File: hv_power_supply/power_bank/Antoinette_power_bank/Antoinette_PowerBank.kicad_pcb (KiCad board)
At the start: 2 copper layers, 30.5 x 48.3 mm, 44 parts, among them J1 NanoFit_RA_TH_02, J2 USB-Micro-1981568-1, J3 NanoFit_RA_TH_02, J4 USB-A-S-X-X-SM2, J5 NanoFit_RA_TH_02, Q1 SSM3K333R, U2 MCP73871T-2CCI_ML, U3 TPS61090RSAR

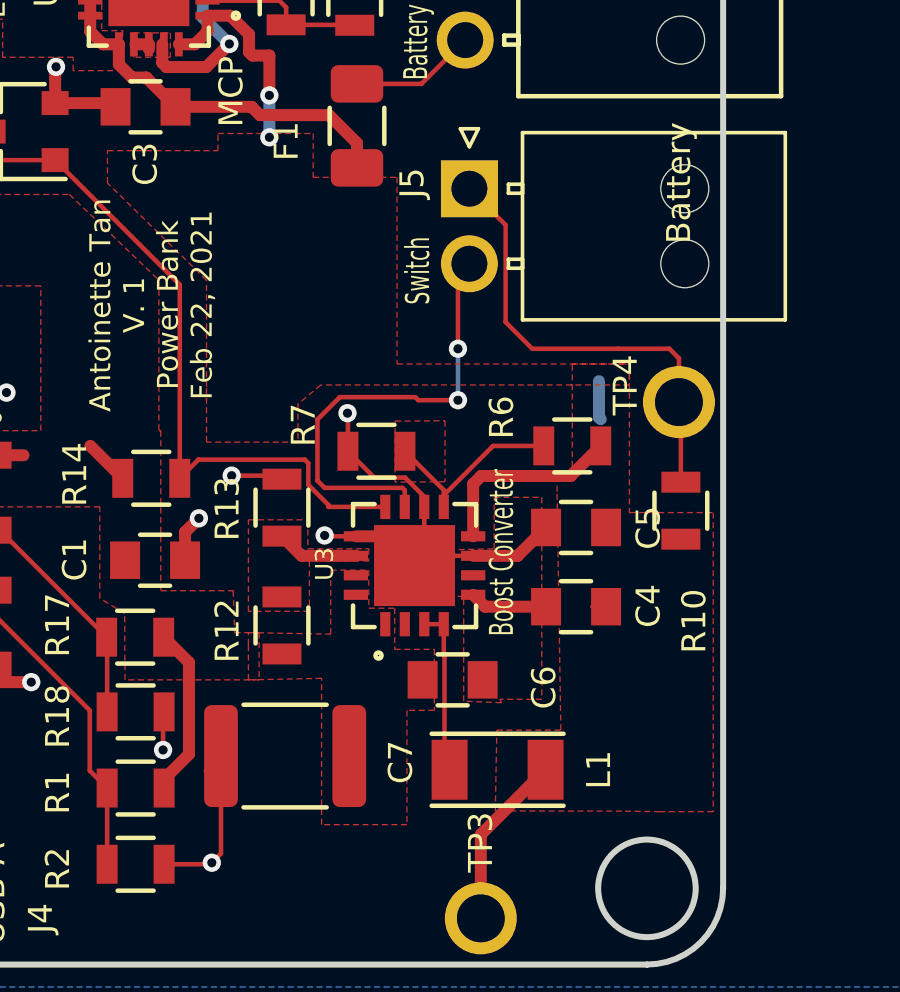
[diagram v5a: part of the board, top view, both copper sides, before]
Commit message: fixed library typos and adjusted silkscreen
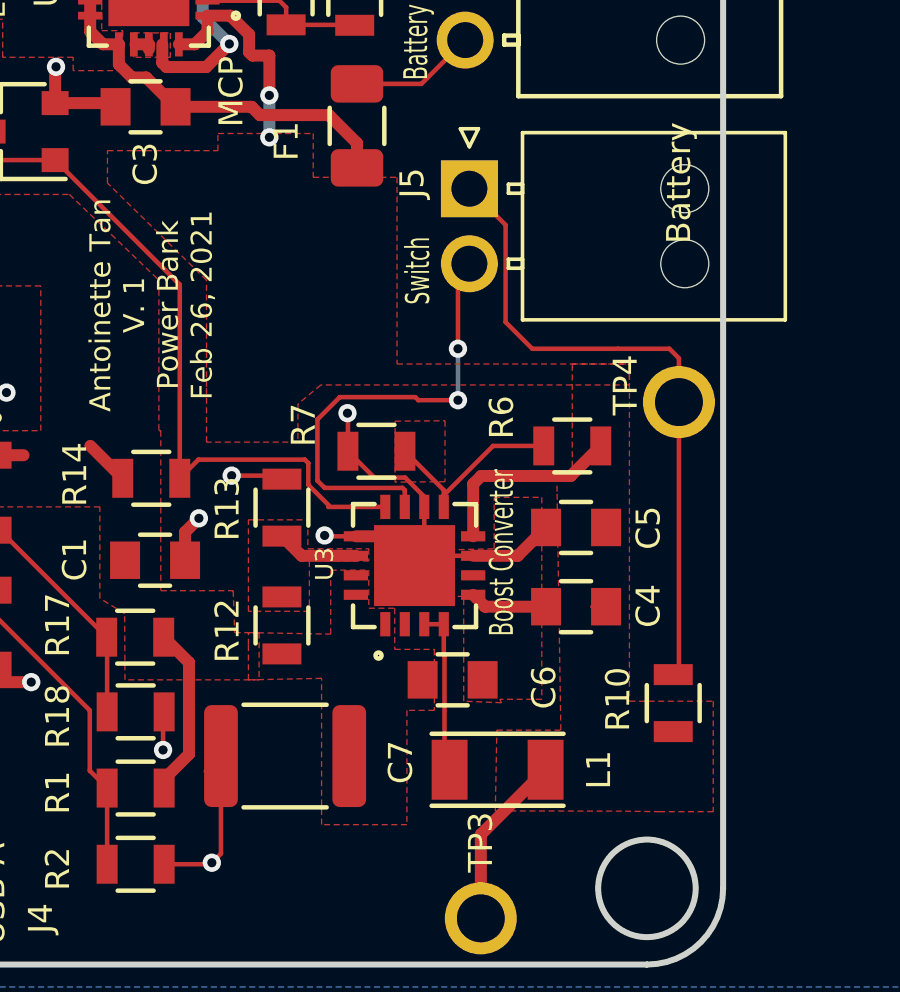
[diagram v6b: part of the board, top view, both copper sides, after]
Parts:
- moved R10 6.42 mm to (98.9, 69.3)
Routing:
- net Net-(J5-Pad1): track 15.6 -> 22.2 mm
- net +BATT: track 20.9 -> 19.6 mm
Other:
- board text added: "Antoinette Tan V. 1 Power Bank Feb 26, 2021"
- board text removed: "Antoinette Tan V. 1 Power Bank Feb 22, 2021"
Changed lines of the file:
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@@
     (thickness 1.6)
     (drawings 23)
-    (tracks 290)
+    (tracks 289)
     (zones 0)
     (modules 44)
@@
   )
   (module footprints:R_0805_OEM (layer F.Cu)
-    (at 99.187 62.865 90)
+    (at 98.933 69.2785 90)
     (descr "Resistor SMD 0805, reflow soldering, Vishay (see dcrcw.pdf)")
     (tags "resistor 0805")
     (attr smd)
-    (fp_text reference R10 (at -3.683 0.4445 90) (layer F.SilkS)
+    (fp_text reference R10 (at 0.127 -1.8415 90) (layer F.SilkS)
       (effects (font (size 0.8 0.8) (thickness 0.15)))
     )
@@
     (effects (font (size 0.8 0.5) (thickness 0.125)))
   )
-  (gr_text "Antoinette Tan\nV. 1\nPower Bank \nFeb 22, 2021\n" (at 81.534 56.007 90) (layer F.SilkS)
+  (gr_text "Antoinette Tan\nV. 1\nPower Bank \nFeb 26, 2021\n" (at 81.534 56.007 90) (layer F.SilkS)
     (effects (font (size 0.7 0.7) (thickness 0.175)))
   )
@@
   (segment (start 92.531499 61.708401) (end 92.2647 61.9752) (width 0.4) (layer F.Cu) (net 5))
   (segment (start 92.2647 63.7188) (end 92.2647 61.9752) (width 0.4) (layer F.Cu) (net 5))
-  (segment (start 96.4565 59.7535) (end 96.5175 59.8145) (width 0.4) (layer B.Cu) (net 5))
-  (segment (start 96.4565 58.547) (end 96.4565 59.7535) (width 0.4) (layer B.Cu) (net 5))
   (segment (start 84.167058 46.3644) (end 83.408799 46.3644) (width 0.4) (layer F.Cu) (net 5))
   (segment (start 84.794701 46.992043) (end 84.167058 46.3644) (width 0.4) (layer F.Cu) (net 5))
@@
   (segment (start 91.2847 66.6488) (end 91.2847 67.672318) (width 0.1524) (layer F.Cu) (net 27))
   (segment (start 99.187 59.309) (end 99.1235 59.2455) (width 0.1524) (layer F.Cu) (net 28))
-  (segment (start 99.187 61.915) (end 99.187 59.309) (width 0.1524) (layer F.Cu) (net 28))
   (segment (start 98.958399 59.080399) (end 99.1235 59.2455) (width 0.1524) (layer F.Cu) (net 28))
   (segment (start 99.1235 59.2455) (end 99.1235 57.785) (width 0.1524) (layer F.Cu) (net 28))
@@
   (segment (start 93.345 56.5785) (end 93.345 53.34) (width 0.15) (layer F.Cu) (net 28))
   (segment (start 97.0915 57.4675) (end 94.234 57.4675) (width 0.1524) (layer F.Cu) (net 28))
+  (segment (start 99.1235 68.138) (end 98.933 68.3285) (width 0.1524) (layer F.Cu) (net 28))
+  (segment (start 99.1235 59.2455) (end 99.1235 68.138) (width 0.1524) (layer F.Cu) (net 28))
   (segment (start 89.9847 62.7388) (end 89.9847 62.408798) (width 0.15) (layer F.Cu) (net 29))
   (segment (start 89.9847 62.1814) (end 89.908499 62.105199) (width 0.1524) (layer F.Cu) (net 29))
@@
       (pts
         (xy 93.0021 72.8726) (xy 93.0529 70.1802) (xy 95.1865 70.1802) (xy 95.0595 62.23) (xy 95.0595 61.722)
-        (xy 95.5675 61.722) (xy 95.5675 57.9755) (xy 97.4725 57.9755) (xy 97.4725 62.9285) (xy 100.2665 62.9285)
+        (xy 95.5675 61.722) (xy 95.5675 57.9755) (xy 97.4725 57.9755) (xy 97.4725 69.215) (xy 100.2665 69.215)
         (xy 100.2665 72.898) (xy 98.4885 72.898) (xy 97.2185 72.87963)
       )

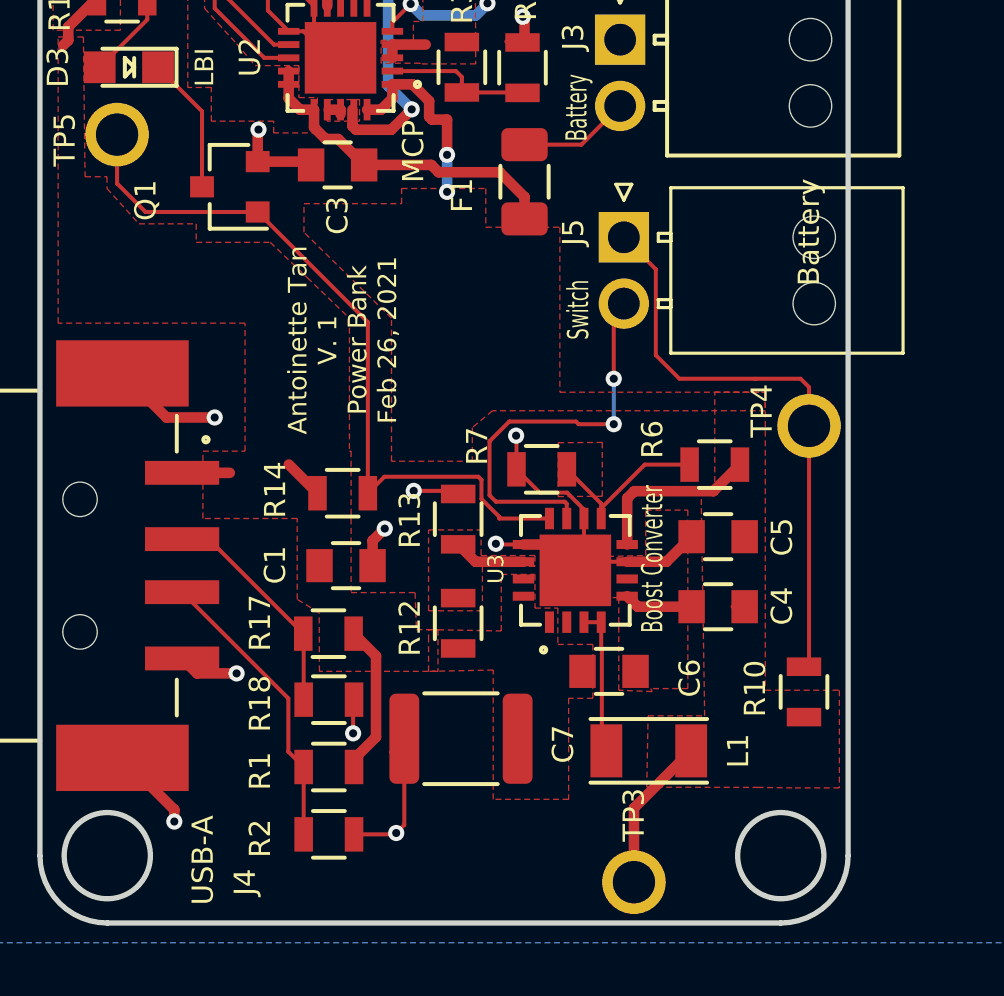
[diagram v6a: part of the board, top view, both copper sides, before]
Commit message: make silkscreen more legible
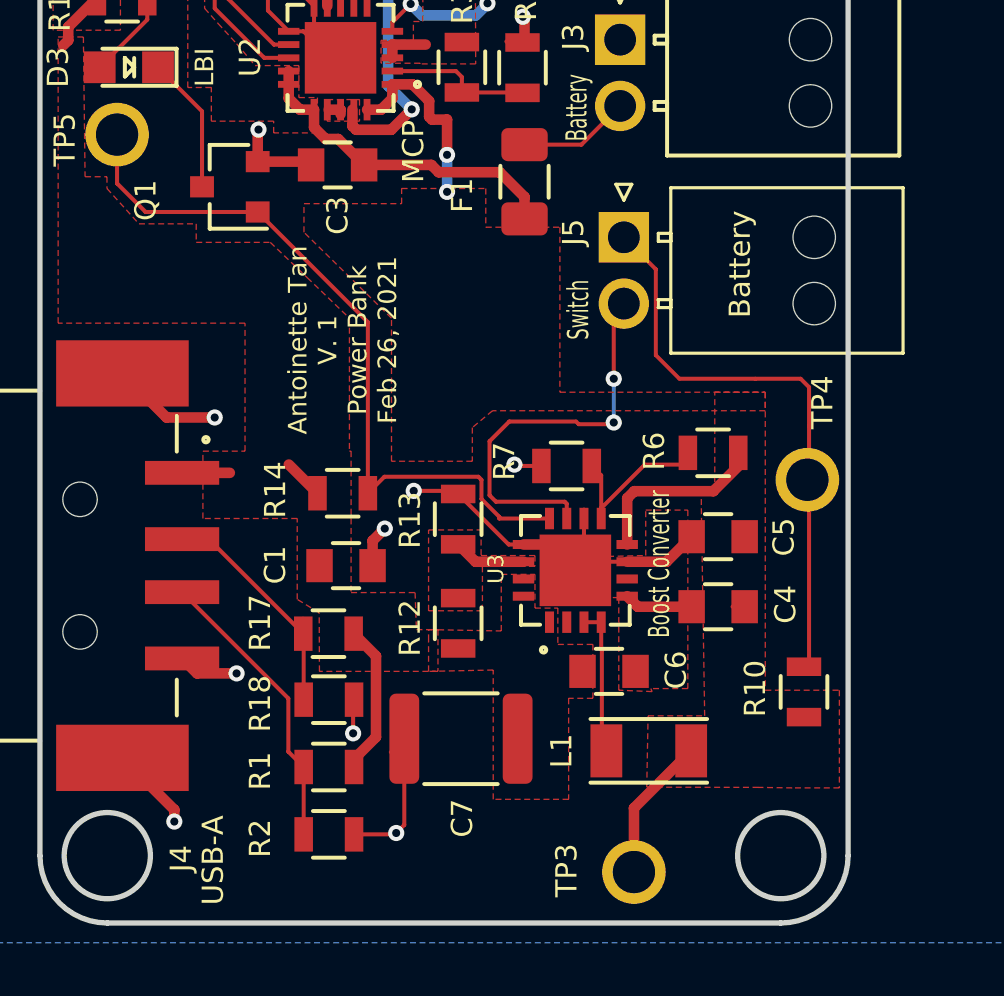
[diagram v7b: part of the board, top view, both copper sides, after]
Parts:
- moved TP4 2.03 mm to (99.1, 61.3)
- moved R7 0.95 mm to (90.0, 60.8)
- moved R6 0.45 mm to (95.5, 60.3)
- moved TP3 0.38 mm to (92.5, 76.1)
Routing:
- net GND: track 76.2 -> 75.0 mm, vias 16 -> 15
- removed copper zone on F.Cu, net Net-(R6-Pad2)
